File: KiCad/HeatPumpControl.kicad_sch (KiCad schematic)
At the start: 34 parts, among them J1 Conn_01x04_Male, J2 Conn_01x04_Male, J3 Conn_01x04_Male, Q1 2N2222A, U1 TSOP23xx, U2 SeedStudio XIAO ESP32 C3 v1

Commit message: Fixed Q1 pinout and grounding fills
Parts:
- Q1: symbol Device:Q_NPN_EBC -> Device:Q_NPN_BEC
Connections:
- net LED1: now also Q1.2 (E); no longer Q1.1 (E)
- net RX: no longer D9.2 (A), J3.2 (Pin_2), R12.2
- net TX: no longer D8.1 (K), J3.1 (Pin_1)
- net at D4.2 (A), R4.2: now also Q1.1 (B); no longer Q1.2 (B)
- new net: D9.2 (A), J3.2 (Pin_2), R12.2
- new net: D8.1 (K), J3.1 (Pin_1)
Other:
- note added: "GPIO2 - PULLED UP - N/A GPIO3/A1 - General IO, no pull-uo GPIO4 - IR out GPIO5 - PIR, 1-Wire, open drain/collector, any pulled up GPIO6 - I2C SDA GPIO7 - I2C SCL GPIO8 - PULLED UP - N/A GPIO9 - ILED GPIO10 - PIR, 1-Wire, open drain/collector, any pulled up GPIO20 - RX <--> TX GPIO21 - TX <--> RX"
- note removed: "GPIO2 - PULLED UP - N/A GPIO3/A1 - General IO, no pull-uo GPIO4 - IR out GPIO5 - PIR, 1-Wire, open drain/collector, any pulled up GPIO6 - I2C SDA GPIO7 - I2C SCL GPIO8 - PULLED UP - N/A GPIO9 - ILED GPIO10 - PIR, 1-Wire, open drain/collector, any pulled up GPIO21 - RX <--> TX GPIO21 - TX <--> RX"

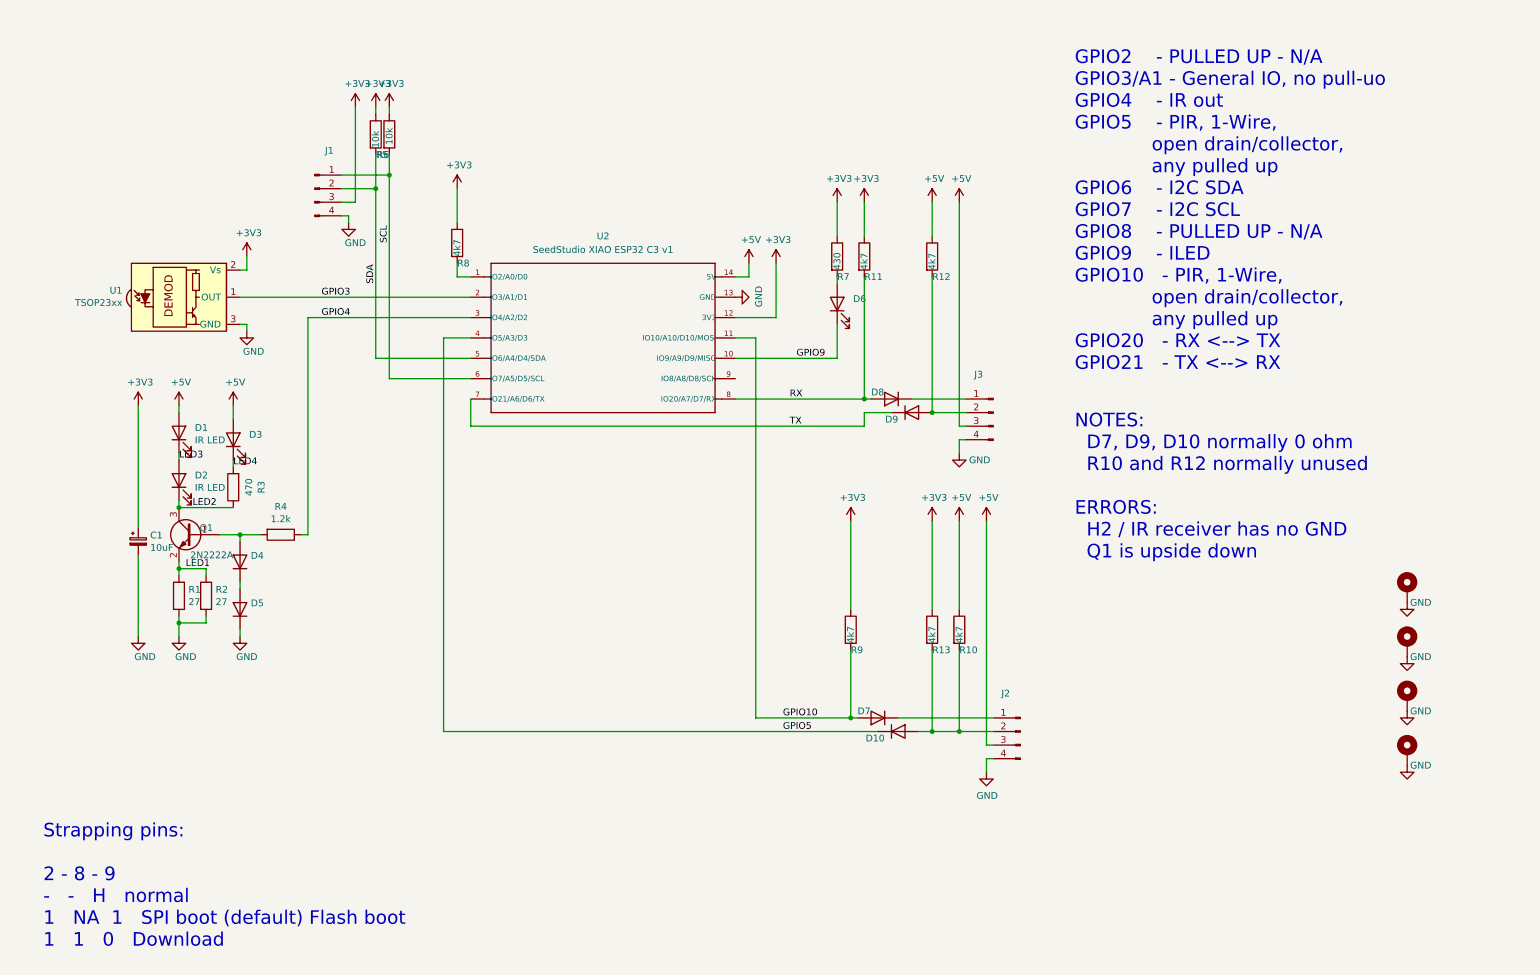
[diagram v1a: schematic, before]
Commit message: ESP32C6 support
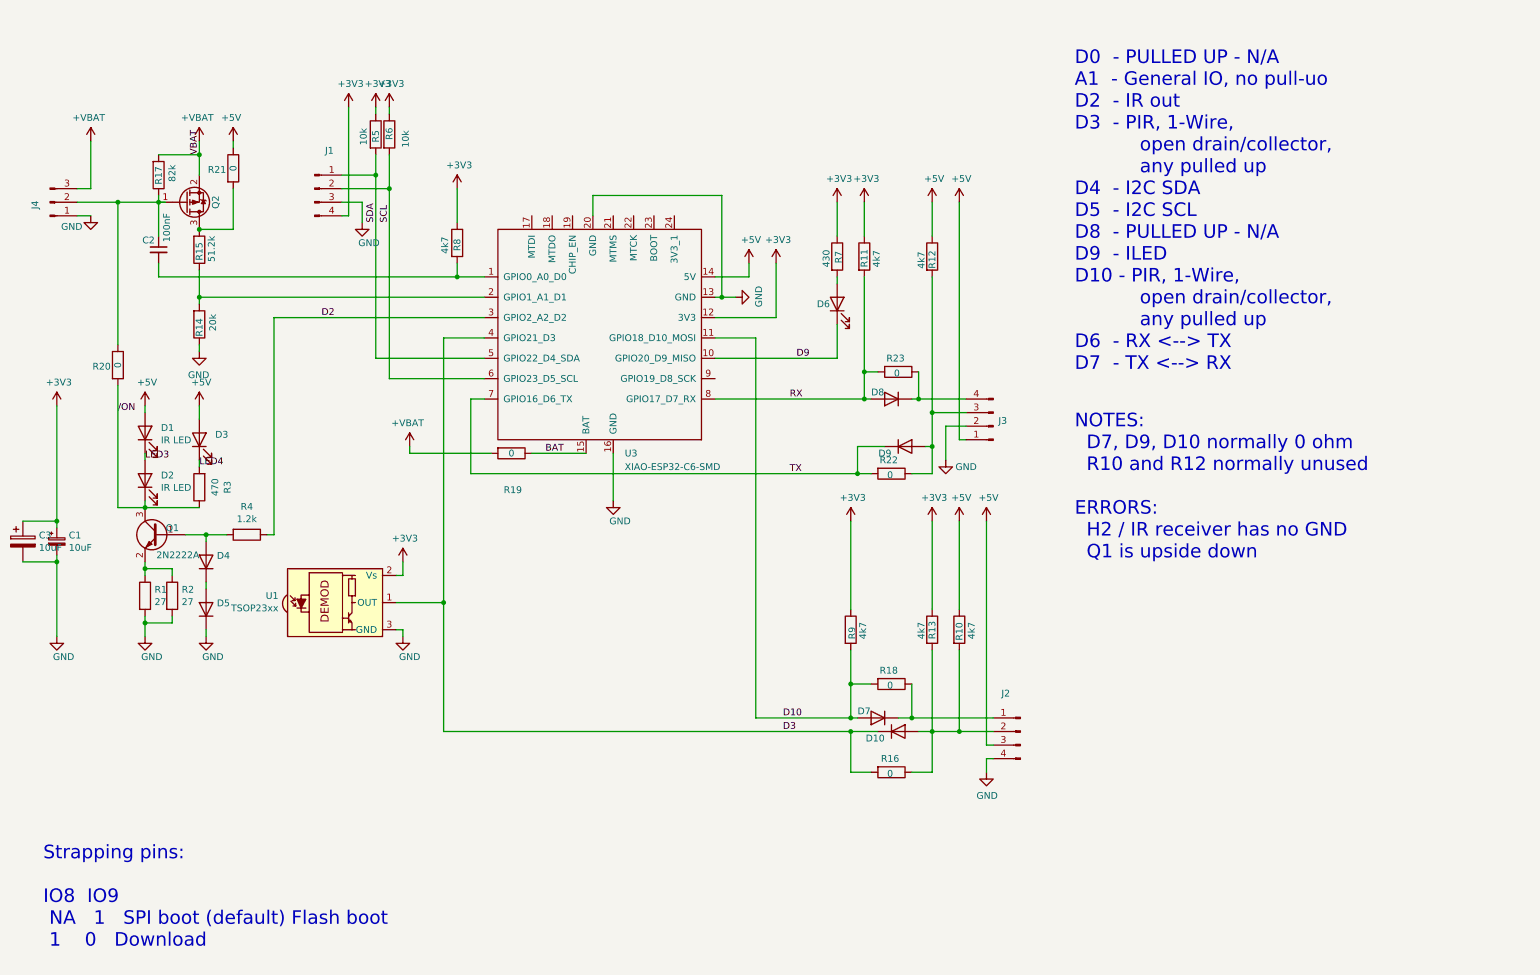
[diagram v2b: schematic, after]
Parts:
- removed H1, H2, H3, H4: MountingHole_Pad, MountingHole:MountingHole_3.2mm_M3_ISO14580_Pad, symbol Mechanical:MountingHole_Pad
- removed U2: SeedStudio XIAO ESP32 C3 v1, LOCAL1:XIAO_ESP32C3_THT, symbol LOCAL1:XIAO_ESP32C3_THT
- added C2: 100nF, Capacitor_SMD:C_0805_2012Metric_Pad1.18x1.45mm_HandSolder, symbol Device:C_Small
- added C3: 10uF, Capacitor_SMD:C_1206_3216Metric_Pad1.33x1.80mm_HandSolder, symbol Device:CP
- added J4: Conn_01x03_Male, Connector_PinHeader_2.54mm:PinHeader_1x03_P2.54mm_Vertical, symbol Connector:Conn_01x03_Pin
- added Q2: Q_PMOS_GDS, Package_TO_SOT_SMD:SOT-23_Handsoldering, symbol Transistor_FET:IRLML6402
- added R14: 20k, Resistor_SMD:R_0805_2012Metric_Pad1.20x1.40mm_HandSolder, symbol Device:R
- added R15: 51.2k, Resistor_SMD:R_0805_2012Metric_Pad1.20x1.40mm_HandSolder, symbol Device:R
- added R16, R18, R19, R20, R21, R22, R23: 0, Resistor_SMD:R_0805_2012Metric, symbol Device:R
- added R17: 82k, Resistor_SMD:R_0805_2012Metric_Pad1.20x1.40mm_HandSolder, symbol Device:R
- added U3: XIAO-ESP32-C6-SMD, LOCAL1:XIAO-ESP32-C6-SMD, symbol LOCAL1:XIAO-ESP32-C6-SMD
- U1: now left out of the parts list
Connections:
- net GPIO5 is gone; now on net D3: D10.1 (K)
- net +3V3: now also J1.4 (Pin_4), C3.1, U3.12 (3V3); no longer J1.3 (Pin_3)
- net +5V: now also J3.1 (Pin_1), R21.1, U3.14 (5V); no longer J3.3 (Pin_3)
- net GND: now also J1.3 (Pin_3), J3.2 (Pin_2), C3.2, J4.1 (Pin_1), R14.1, U3.13 (GND), U3.16 (GND), U3.20 (GND); no longer J1.4 (Pin_4), J3.4 (Pin_4)
- net RX: now also R23.2, U3.8 (GPIO17_D7_RX)
- net SCL: now also J1.2 (Pin_2), U3.6 (GPIO23_D5_SCL); no longer J1.1 (Pin_1)
- net SDA: now also J1.1 (Pin_1), U3.5 (GPIO22_D4_SDA); no longer J1.2 (Pin_2)
- net TX: now also R22.2, U3.7 (GPIO16_D6_TX)
- net at D9.2 (A), R12.2: now also J3.3 (Pin_3), R22.1; no longer J3.2 (Pin_2)
- net at D8.1 (K): now also J3.4 (Pin_4), R23.1; no longer J3.1 (Pin_1)
- net at D10.2 (A), J2.2 (Pin_2), R10.2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: now also R16.1
- net at D7.1 (K), J2.1 (Pin_1): now also R18.1
- net at R8.2: now also C2.2, U3.1 (GPIO0_A0_D0)
- net GPIO10 renamed D10
- net D10: now also R18.2, U3.11 (GPIO18_D10_MOSI)
- net GPIO3 renamed D3
- net D3: now also R16.2, U3.4 (GPIO21_D3)
- net GPIO4 renamed D2
- net D2: now also U3.3 (GPIO2_A2_D2)
- net GPIO9 renamed D9
- net D9: now also U3.10 (GPIO20_D9_MISO)
- net LED1: no longer names the net of Q1.2 (E), R1.1, R2.1
- net LED2 renamed /ON
- net /ON: now also R20.2
- new net: R14.2, R15.1, U3.2 (GPIO1_A1_D1)
- new net: C2.1, J4.2 (Pin_2), Q2.1 (G), R17.1, R20.1
- new net: Q2.3 (D), R15.2, R21.2
- new net +VBAT: J4.3 (Pin_3), Q2.2 (S), R17.2, R19.2
- new net BAT: R19.1, U3.15 (BAT)
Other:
- note added: "D0 - PULLED UP - N/A A1 - General IO, no pull-uo D2 - IR out D3 - PIR, 1-Wire, open drain/collector, any pulled up D4 - I2C SDA D5 - I2C SCL D8 - PULLED UP - N/A D9 - ILED D10 - PIR, 1-Wire, open drain/collector, any pulled up D6 - RX <--> TX D7 - TX <--> RX"
- note added: "Strapping pins: IO8 IO9 NA 1 SPI boot (default) Flash boot 1 0 Download"
- note removed: "GPIO2 - PULLED UP - N/A GPIO3/A1 - General IO, no pull-uo GPIO4 - IR out GPIO5 - PIR, 1-Wire, open drain/collector, any pulled up GPIO6 - I2C SDA GPIO7 - I2C SCL GPIO8 - PULLED UP - N/A GPIO9 - ILED GPIO10 - PIR, 1-Wire, open drain/collector, any pulled up GPIO20 - RX <--> TX GPIO21 - TX <--> RX"
- note removed: "Strapping pins: 2 - 8 - 9 - - H normal 1 NA 1 SPI boot (default) Flash boot 1 1 0 Download"
- moved on the sheet: C1, D1, D2, D3, D4, D5, D9, J3, Q1, R1, R2, R3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

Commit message: Add 5-3.3 V divider for Rx
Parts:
- added R24: 3k3, Resistor_SMD:R_0805_2012Metric, symbol Device:R
- R23: value 0 -> 18k
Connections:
- net GND: now also R24.2
- net RX: now also R24.1
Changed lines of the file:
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@@
 	)
 	(junction
+		(at 163.83 90.17)
+		(diameter 0)
+		(color 0 0 0 0)
+	)
+	(junction
 		(at 38.1 110.49)
 		(diameter 0)
@@
 	(wire
 		(pts
-			(xy 144.78 90.17) (xy 172.72 90.17)
+			(xy 144.78 90.17) (xy 163.83 90.17)
 		)
 		(stroke
@@
 	(wire
 		(pts
+			(xy 163.83 90.17) (xy 172.72 90.17)
+		)
+		(stroke
+			(width 0)
+			(type default)
+		)
+	)
+	(wire
+		(pts
 			(xy 62.23 74.93) (xy 101.6 74.93)
 		)
@@
 	(wire
 		(pts
+			(xy 163.83 90.17) (xy 163.83 91.44)
+		)
+		(stroke
+			(width 0)
+			(type default)
+		)
+	)
+	(wire
+		(pts
 			(xy 87.63 100.33) (xy 87.63 99.06)
 		)
@@
 			)
 		)
-		(property "Value" "0"
+		(property "Value" "18k"
 			(at 178.816 85.344 90)
 			(effects
@@
 	)
 	(symbol
+		(lib_id "power:GND")
+		(at 163.83 99.06 0)
+		(unit 1)
+		(exclude_from_sim no)
+		(in_bom yes)
+		(on_board yes)
+		(dnp no)
+		(property "Reference" "#PWR026"
+			(at 163.83 105.41 0)
+			(effects
+				(font
+					(size 1.27 1.27)
+				)
+				(hide yes)
+			)
+		)
+		(property "Value" "GND"
+			(at 165.1 102.87 0)
+			(effects
+				(font
+					(size 1.27 1.27)
+				)
+			)
+		)
+		(property "Footprint" ""
+			(at 163.83 99.06 0)
+			(effects
+				(font
+					(size 1.27 1.27)
+				)
+				(hide yes)
+			)
+		)
+		(property "Datasheet" ""
+			(at 163.83 99.06 0)
+			(effects
+				(font
+					(size 1.27 1.27)
+				)
+				(hide yes)
+			)
+		)
+		(property "Description" ""
+			(at 163.83 99.06 0)
+			(effects
+				(font
+					(size 1.27 1.27)
+				)
+				(hide yes)
+			)
+		)
+		(pin "1"
+		)
+		(instances
+			(project "HeatPumpControl"
+				(path "/2a5b3e3c-2022-46db-8938-2c3b2e9edb6d"
+					(reference "#PWR026")
+					(unit 1)
+				)
+			)
+		)
+	)
+	(symbol
 		(lib_id "power:+3.3V")
 		(at 172.72 53.34 0)
@@
 					(unit 1)
 				)
+			)
+		)
+	)
+	(symbol
+		(lib_id "Device:R")
+		(at 163.83 95.25 0)
+		(unit 1)
+		(exclude_from_sim no)
+		(in_bom yes)
+		(on_board yes)
+		(dnp no)
+		(property "Reference" "R24"
+			(at 163.83 97.282 90)
+			(effects
+				(font
+					(size 1.27 1.27)
+				)
+				(justify left)
+			)
+		)
+		(property "Value" "3k3"
+			(at 166.116 97.282 90)
+			(effects
+				(font
+					(size 1.27 1.27)
+				)
+				(justify left)
+			)
+		)
+		(property "Footprint" "Resistor_SMD:R_0805_2012Metric"
+			(at 162.052 95.25 90)
+			(effects
+				(font
+					(size 1.27 1.27)
+				)
+				(hide yes)
+			)
+		)
+		(property "Datasheet" "~"
+			(at 163.83 95.25 0)
+			(effects
+				(font
+					(size 1.27 1.27)
+				)
+				(hide yes)
+			)
+		)
+		(property "Description" ""
+			(at 163.83 95.25 0)
+			(effects
+				(font
+					(size 1.27 1.27)
+				)
+				(hide yes)
+			)
+		)
+		(pin "1"
+		)
+		(pin "2"
+		)
+		(instances
+			(project "HeatPumpControl"
+				(path "/2a5b3e3c-2022-46db-8938-2c3b2e9edb6d"
+					(reference "R24")
+					(unit 1)
+				)

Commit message: Added combined C3/C6 module footprint
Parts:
- removed D8: 1N4148, Diode_SMD:D_MiniMELF, symbol Diode:1N4148
- removed R11: 4k7, Resistor_SMD:R_0805_2012Metric, symbol Device:R
- added D11: 1N4148, Diode_SMD:D_SOD-323, symbol Diode:1N4148
- D4, D5, D7: footprint Diode_SMD:D_MiniMELF -> Diode_SMD:D_SOD-323
- Q1: footprint Package_TO_SOT_SMD:SOT-23 -> Package_TO_SOT_SMD:SOT-23_Handsoldering
- R23: value 18k -> 2.2k
- R24: value 3k3 -> 4.3k
- U3: footprint LOCAL1:XIAO-ESP32-C6-SMD -> LOCAL1:XIAO-ESP32-C3C6-SMD
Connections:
- net +3V3: now also D11.1 (K)
- net +5V: now also J2.2 (Pin_2); no longer J2.3 (Pin_3)
- net GND: now also J2.1 (Pin_1); no longer J2.4 (Pin_4)
- net TX: now also D11.2 (A)
- net at D7.1 (K), R18.1: now also J2.4 (Pin_4); no longer J2.1 (Pin_1)
- net at D10.2 (A), R10.2, R13.2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: now also J2.3 (Pin_3); no longer J2.2 (Pin_2)
- net /ON renamed ON
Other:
- moved on the sheet: J2, R23

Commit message: Manufacturing for v4.0
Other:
- title: Heat pump serial and IR interface -> Heat pump ctrl / generic IO 
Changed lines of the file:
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@@
 	(paper "A4")
 	(title_block
-		(title "Heat pump serial and IR interface")
-		(date "2025-10-02")
+		(title "Heat pump ctrl / generic IO ")
+		(date "2025-10-28")
 		(rev "v4.0")
 		(company "Hans Rune Bue <email@hansrune.net>")
